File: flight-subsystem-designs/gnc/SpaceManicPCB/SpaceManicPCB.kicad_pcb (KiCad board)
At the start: 4 copper layers, 90.2 x 96.1 mm, 28 parts, among them Q1 EPC2014C

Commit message: Final Changes
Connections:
- H1 pad 41: /I2C1_SDA -> unconnected-(H1-Pin_41-Pad41)
- H1 pad 43: /I2C1_SCL -> unconnected-(H1-Pin_43-Pad43)
- H17 pad 13: /I2C1_SDA -> unconnected-(H17-Pin_13-Pad13)
- H17 pad 14: /I2C1_SCL -> unconnected-(H17-Pin_14-Pad14)
- H18 pad 13: /I2C1_SDA -> unconnected-(H18-Pin_13-Pad13)
- H18 pad 14: /I2C1_SCL -> unconnected-(H18-Pin_14-Pad14)
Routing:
- net /I2C1_SDA: track 84.0 -> 0.00 mm
- net /I2C1_SCL: track 82.4 -> 0.00 mm
- net /GPS Celeste Connector/PPS: track 62.4 -> 70.9 mm

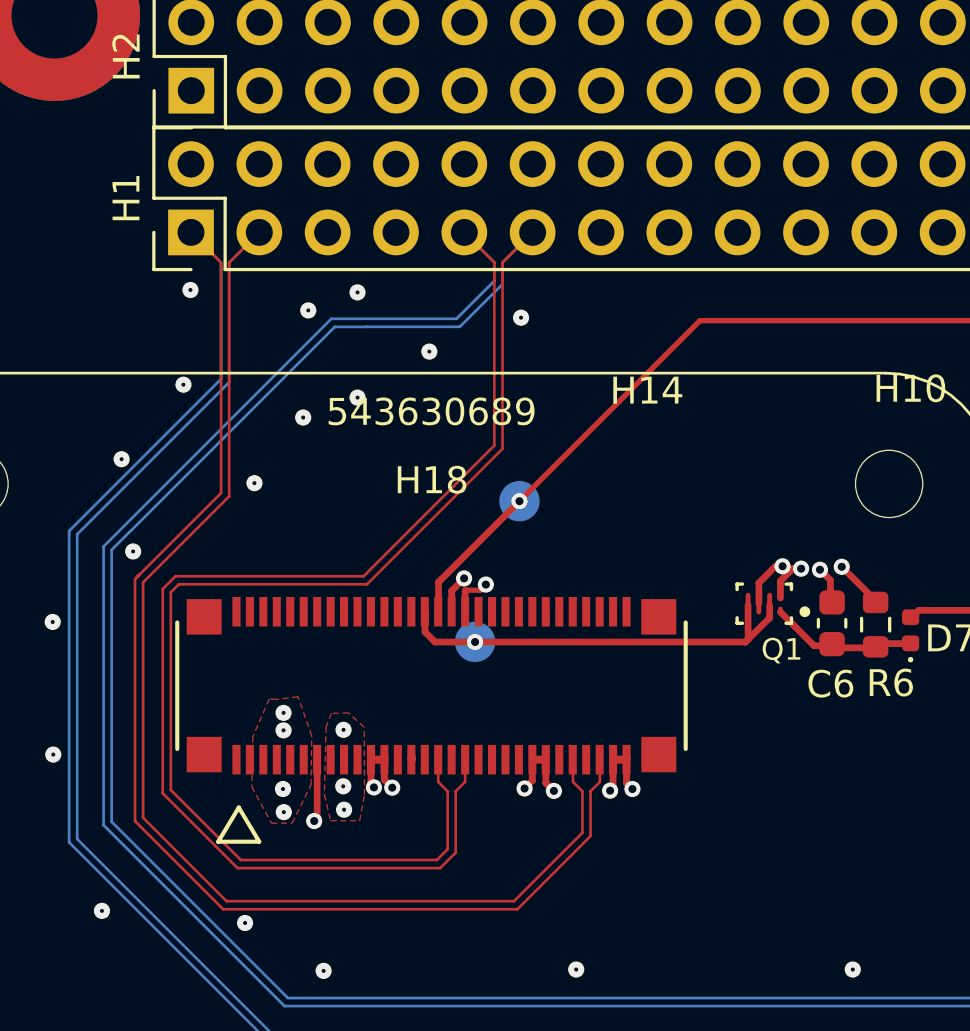
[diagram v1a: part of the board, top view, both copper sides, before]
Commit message: Added UART
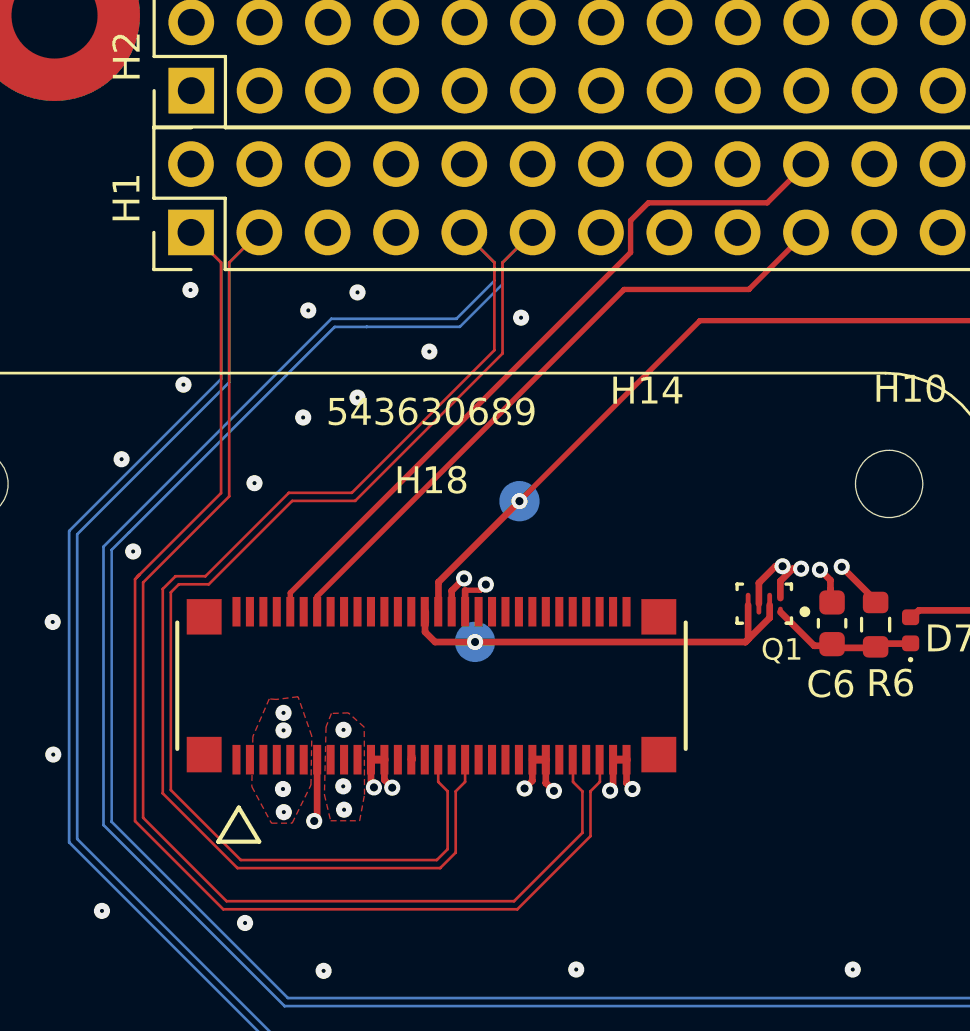
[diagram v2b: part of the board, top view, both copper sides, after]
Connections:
- H1 pad 19: unconnected-(H1-Pin_19-Pad19) -> /GPS Celeste Connector/UART_GPS_RX
- H1 pad 20: unconnected-(H1-Pin_20-Pad20) -> /GPS Celeste Connector/UART_GPS_TX
- H18 pad 35: unconnected-(H18-Pin_35-Pad35) -> /GPS Celeste Connector/UART_GPS_TX
- H18 pad 37: unconnected-(H18-Pin_37-Pad37) -> /GPS Celeste Connector/UART_GPS_RX
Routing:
- net /GPS Celeste Connector/UART_GPS_TX: track 0.00 -> 27.2 mm
- net /GPS Celeste Connector/UART_GPS_RX: track 0.00 -> 24.3 mm
- net /RS485_P: track 143.4 -> 141.3 mm
- net /RS485_N: track 145.4 -> 143.3 mm
